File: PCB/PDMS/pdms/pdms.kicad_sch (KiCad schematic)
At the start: 46 parts, among them IC19 STM32L496ZGT6, IC20 AT25SF128A-SHB-T, J1 DBG, J2 12V_CONN, Y1 48Mhz, Y2 32KHz

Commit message: Mostly assigned footprints
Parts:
- removed J2: 12V_CONN, symbol Connector:Conn_01x01_Male

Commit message: Crucial fully assigned schematics
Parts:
- JP1: footprint (none) -> Jumper:SolderJumper-3_P1.3mm_Open_Pad1.0x1.5mm

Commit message: Added connector and more
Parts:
- added J2: 6473427-1, 64734271, symbol pdms_additional:6473427-1
- C41, C42, C43, C44, C45, C46, C47, C48, C49, C50, C51, C52, C53: footprint Capacitor_SMD:C_0402_1005Metric_Pad0.74x0.62mm_HandSolder -> Resistor_SMD:R_0402_1005Metric
- L1: footprint (none) -> Inductor_SMD:L_0402_1005Metric
- R108, R109, R55, R66: footprint Resistor_SMD:R_0402_1005Metric_Pad0.72x0.64mm_HandSolder -> Resistor_SMD:R_0402_1005Metric
- R54: footprint (none) -> Resistor_SMD:R_0805_2012Metric

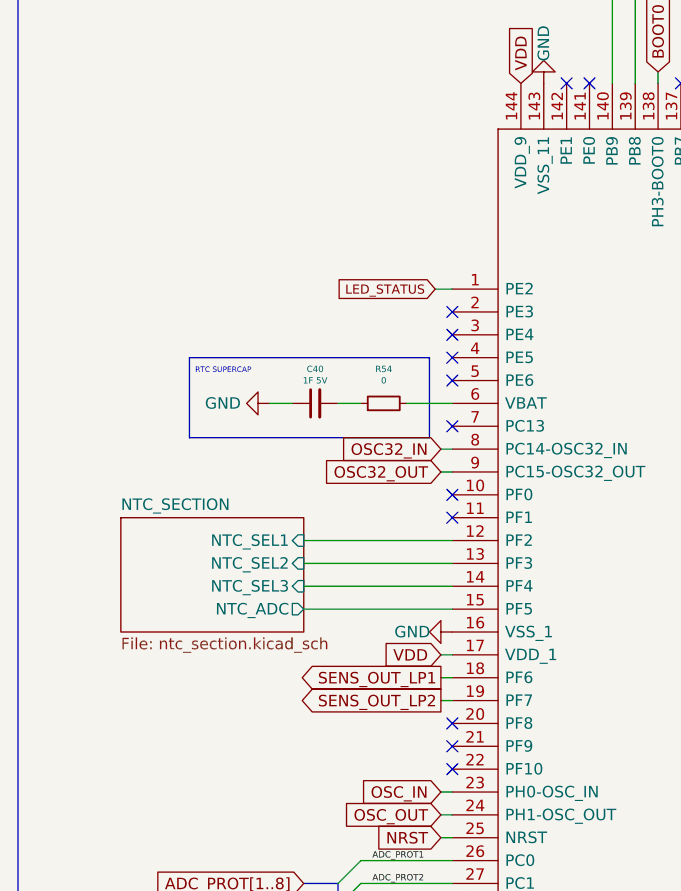
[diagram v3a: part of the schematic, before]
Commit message: Added voltage mux section & layouting high side - hp
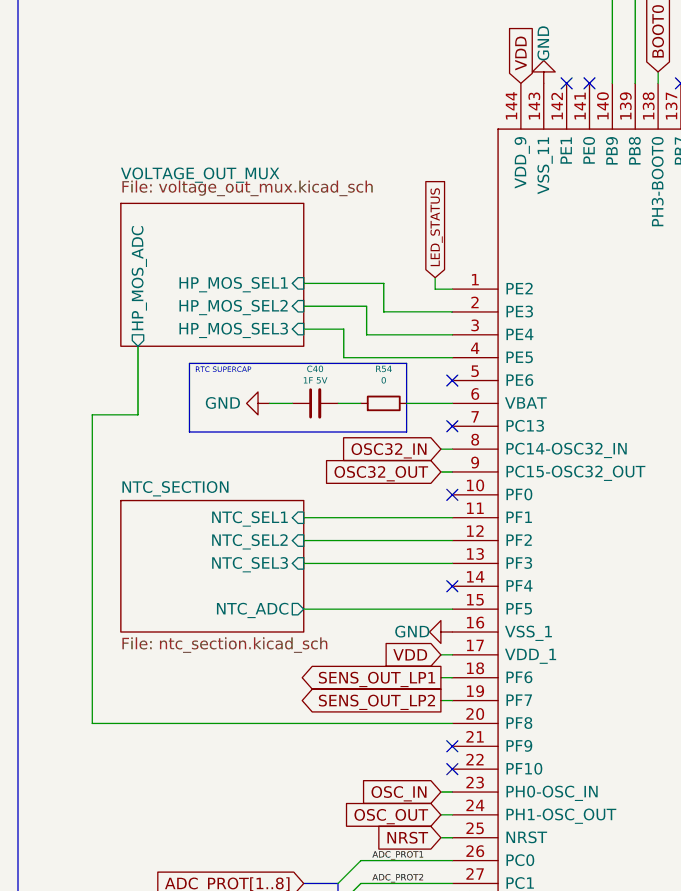
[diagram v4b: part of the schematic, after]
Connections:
- net NTC_SECTION/NTC_SEL1: now also IC19.11 (PF1); no longer IC19.12 (PF2)
- net NTC_SECTION/NTC_SEL2: now also IC19.12 (PF2); no longer IC19.13 (PF3)
- net NTC_SECTION/NTC_SEL3: now also IC19.13 (PF3); no longer IC19.14 (PF4)
- net VOLTAGE_OUT_MUX/HP_MOS_SEL1: now reaches IC19.2 (PE3)
- net VOLTAGE_OUT_MUX/HP_MOS_ADC: now reaches IC19.20 (PF8)
- net VOLTAGE_OUT_MUX/HP_MOS_SEL2: now reaches IC19.3 (PE4)
- net VOLTAGE_OUT_MUX/HP_MOS_SEL3: now reaches IC19.4 (PE5)
- no-connect marks 34 -> 30
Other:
- added sheet VOLTAGE_OUT_MUX (voltage_out_mux.kicad_sch)

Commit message: Medium power stage layout
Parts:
- J2: footprint 64734271 -> (none)
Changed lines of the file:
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@@
   (paper "A3")
   (bus_alias "QUADSPI" (members "CLK" "NCS" "BK1_IO0" "BK1_IO1" "BK1_IO2" "BK1_IO3"))
-  (bus_alias "SPI2" (members "SCK" "MISO" "MOSI"))
-  (bus_alias "SPI1" (members "SCK" "MOSI" "MISO"))
   (bus_alias "SPI3" (members "SCK" "MOSI" "MISO"))
+  (bus_alias "SPI1" (members "SCK" "MOSI" "MISO"))
+  (bus_alias "SPI2" (members "SCK" "MISO" "MOSI"))
   (junction (at 262.89 106.68) (diameter 0) (color 0 0 0 0)
   )
@@
     (property "Reference" "J2" (id 0) (at 368.3 158.75 0))
     (property "Value" "6473427-1" (id 1) (at 368.3 161.29 0))
-    (property "Footprint" "64734271" (id 2) (at 377.19 164.465 0)
+    (property "Footprint" "" (id 2) (at 377.19 164.465 0)
       (effects (font (size 1.27 1.27)) (justify left) hide)
     )
@@
     )
     (path "/1bbf27ea-c2a2-447a-8999-6ade1a66fd07/382312d4-d5fa-4b39-ace5-70b089c5702e/3370c7ea-69b3-4a24-9f00-dcee23cfca4d"
-      (reference "C14") (unit 1) (value "10nF") (footprint "Capacitor_SMD:C_0805_2012Metric")
+      (reference "C14") (unit 1) (value "10nF") (footprint "Capacitor_SMD:C_0603_1608Metric")
     )
     (path "/1bbf27ea-c2a2-447a-8999-6ade1a66fd07/382312d4-d5fa-4b39-ace5-70b089c5702e/ea05a7b0-a751-41e9-9025-7282beaf4e1d"
-      (reference "C15") (unit 1) (value "10nF") (footprint "Capacitor_SMD:C_0805_2012Metric")
+      (reference "C15") (unit 1) (value "10nF") (footprint "Capacitor_SMD:C_0603_1608Metric")
     )
     (path "/1bbf27ea-c2a2-447a-8999-6ade1a66fd07/382312d4-d5fa-4b39-ace5-70b089c5702e/1d67a290-67f8-4c45-a531-ecadc3675a3a"
-      (reference "C16") (unit 1) (value "10nF") (footprint "Capacitor_SMD:C_0805_2012Metric")
+      (reference "C16") (unit 1) (value "10nF") (footprint "Capacitor_SMD:C_0603_1608Metric")
     )
     (path "/1bbf27ea-c2a2-447a-8999-6ade1a66fd07/382312d4-d5fa-4b39-ace5-70b089c5702e/5bf50f4d-56e9-48bb-98a7-9ba919c6cef3"
-      (reference "C17") (unit 1) (value "10nF") (footprint "Capacitor_SMD:C_0805_2012Metric")
+      (reference "C17") (unit 1) (value "10nF") (footprint "Capacitor_SMD:C_0603_1608Metric")
     )
     (path "/1bbf27ea-c2a2-447a-8999-6ade1a66fd07/382312d4-d5fa-4b39-ace5-70b089c5702e/a56d669c-c591-4097-b59f-91a85033a48d"
@@
     )
     (path "/1bbf27ea-c2a2-447a-8999-6ade1a66fd07/3f236385-25de-4e3f-a771-f7ba7d7dd03b/3370c7ea-69b3-4a24-9f00-dcee23cfca4d"
-      (reference "C70") (unit 1) (value "10nF") (footprint "Capacitor_SMD:C_0805_2012Metric")
+      (reference "C70") (unit 1) (value "10nF") (footprint "Capacitor_SMD:C_0603_1608Metric")
     )
     (path "/1bbf27ea-c2a2-447a-8999-6ade1a66fd07/3f236385-25de-4e3f-a771-f7ba7d7dd03b/ea05a7b0-a751-41e9-9025-7282beaf4e1d"
-      (reference "C71") (unit 1) (value "10nF") (footprint "Capacitor_SMD:C_0805_2012Metric")
+      (reference "C71") (unit 1) (value "10nF") (footprint "Capacitor_SMD:C_0603_1608Metric")
     )
     (path "/1bbf27ea-c2a2-447a-8999-6ade1a66fd07/3f236385-25de-4e3f-a771-f7ba7d7dd03b/1d67a290-67f8-4c45-a531-ecadc3675a3a"
-      (reference "C72") (unit 1) (value "10nF") (footprint "Capacitor_SMD:C_0805_2012Metric")
+      (reference "C72") (unit 1) (value "10nF") (footprint "Capacitor_SMD:C_0603_1608Metric")
     )
     (path "/1bbf27ea-c2a2-447a-8999-6ade1a66fd07/3f236385-25de-4e3f-a771-f7ba7d7dd03b/5bf50f4d-56e9-48bb-98a7-9ba919c6cef3"
-      (reference "C73") (unit 1) (value "10nF") (footprint "Capacitor_SMD:C_0805_2012Metric")
+      (reference "C73") (unit 1) (value "10nF") (footprint "Capacitor_SMD:C_0603_1608Metric")
     )
     (path "/f973e110-c9eb-4494-a7eb-37628bac99f8/808924b7-27d2-4209-a500-7d9830d3c986"
@@
     )
     (path "/3e968dc6-4b4f-40cc-bb81-01963d659485"
-      (reference "J2") (unit 1) (value "6473427-1") (footprint "64734271")
+      (reference "J2") (unit 1) (value "6473427-1") (footprint "")
     )
     (path "/2ac18ad3-7152-47d9-8b69-5b63b2971d75"

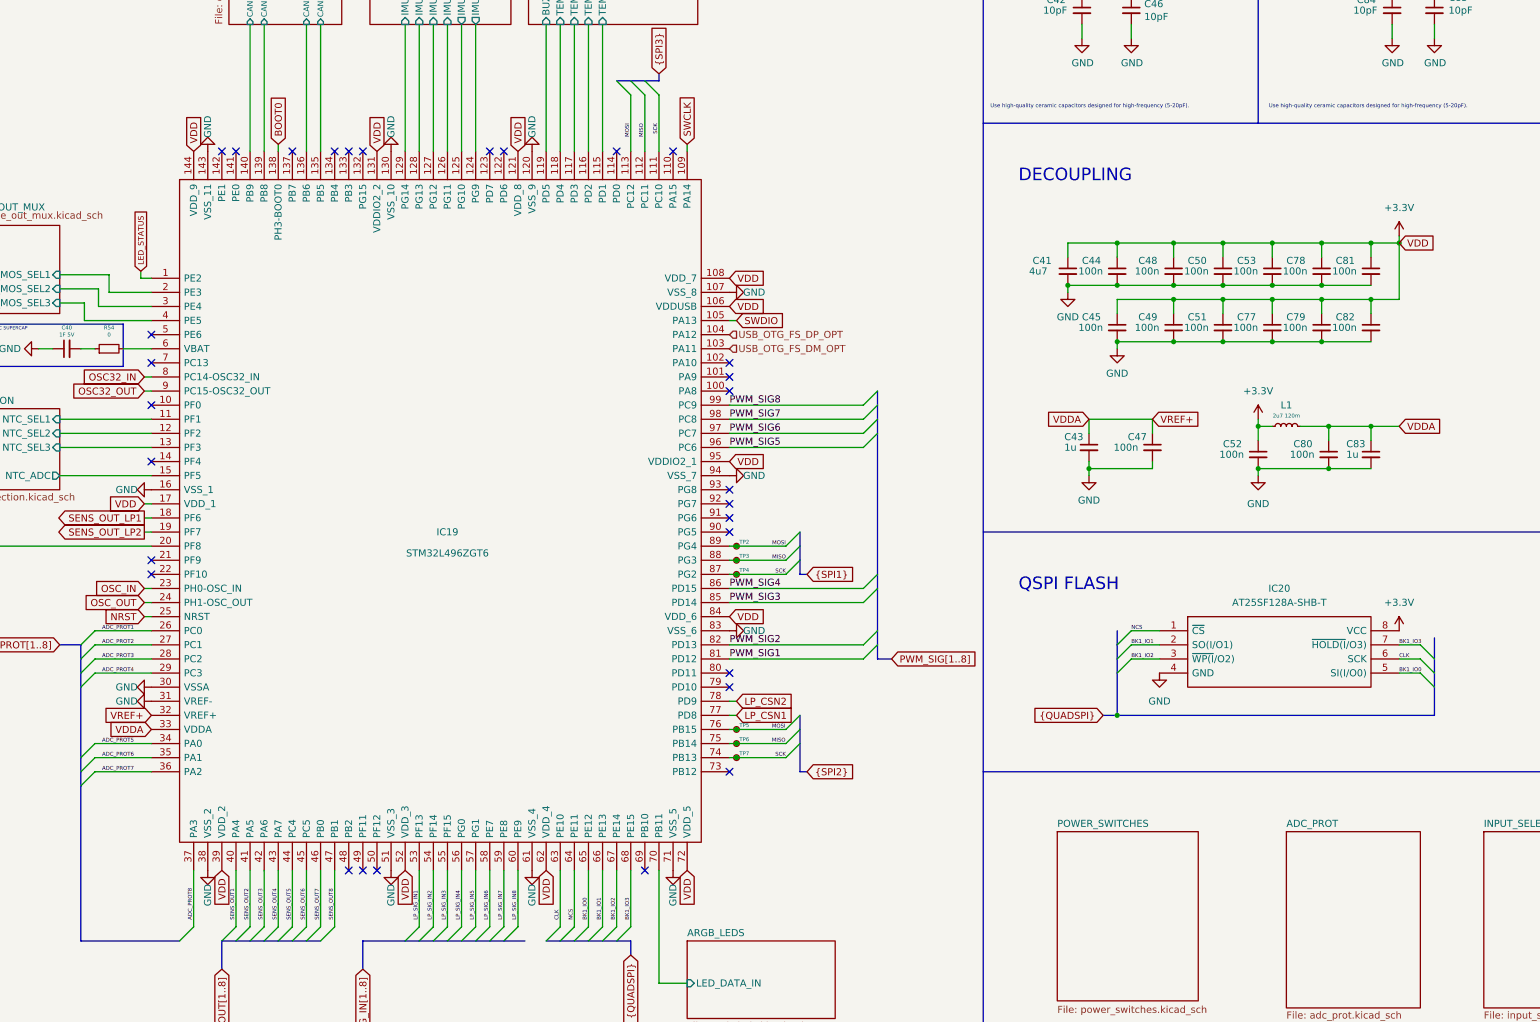
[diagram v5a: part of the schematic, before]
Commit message: Imported 3.3V section with problematic shitty plugin
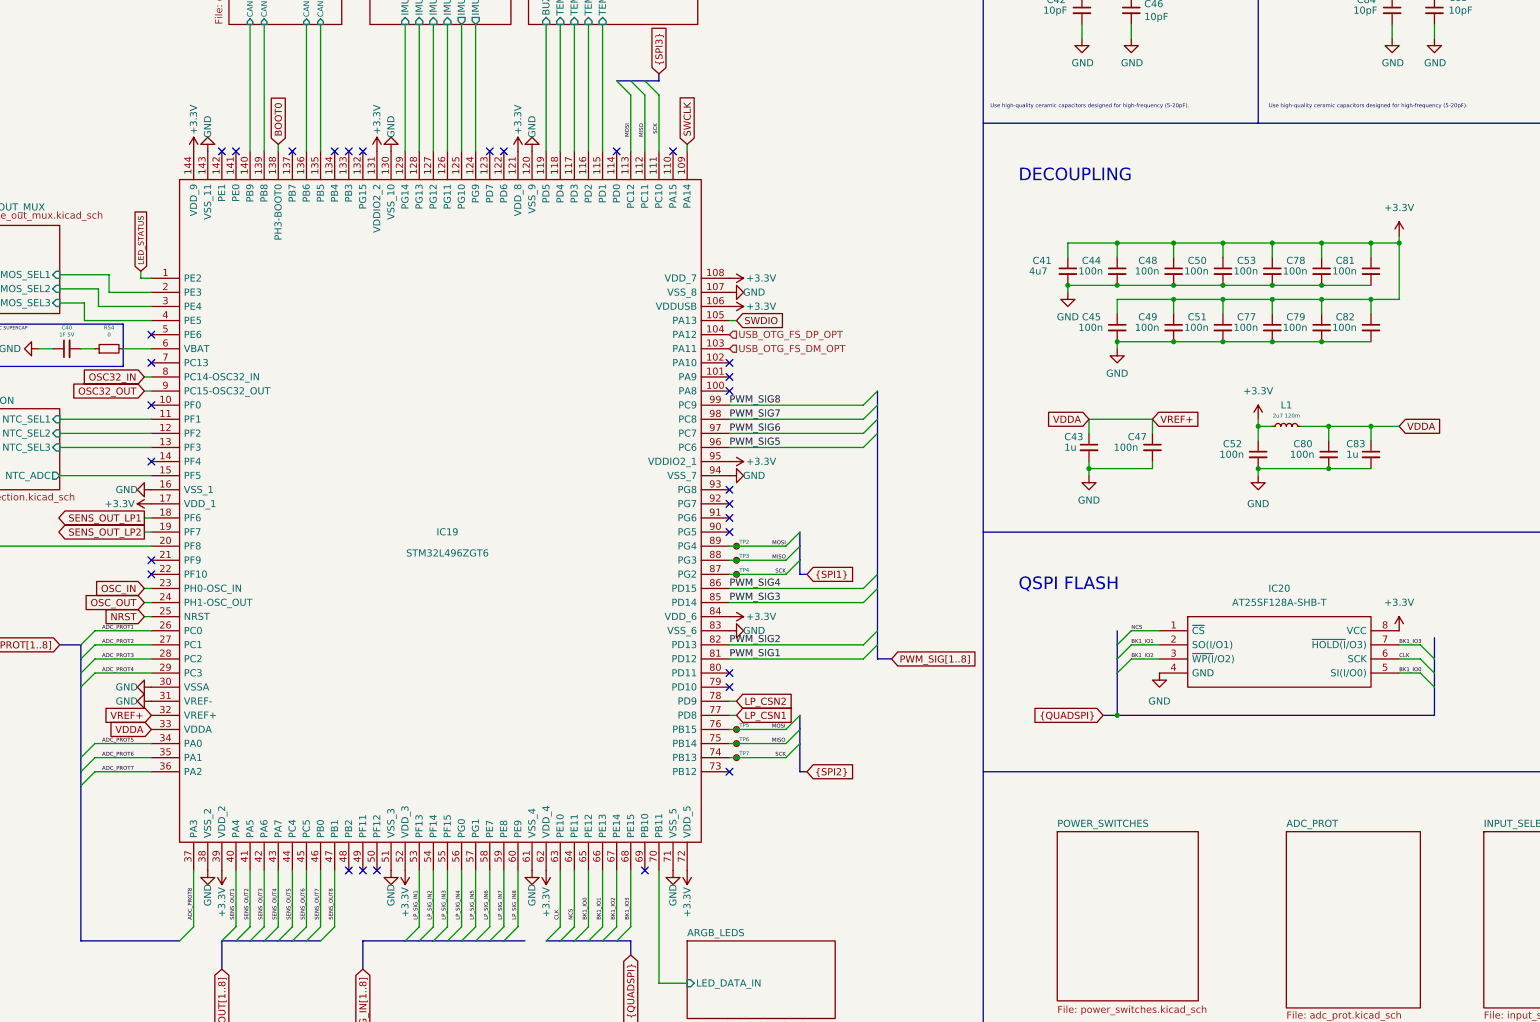
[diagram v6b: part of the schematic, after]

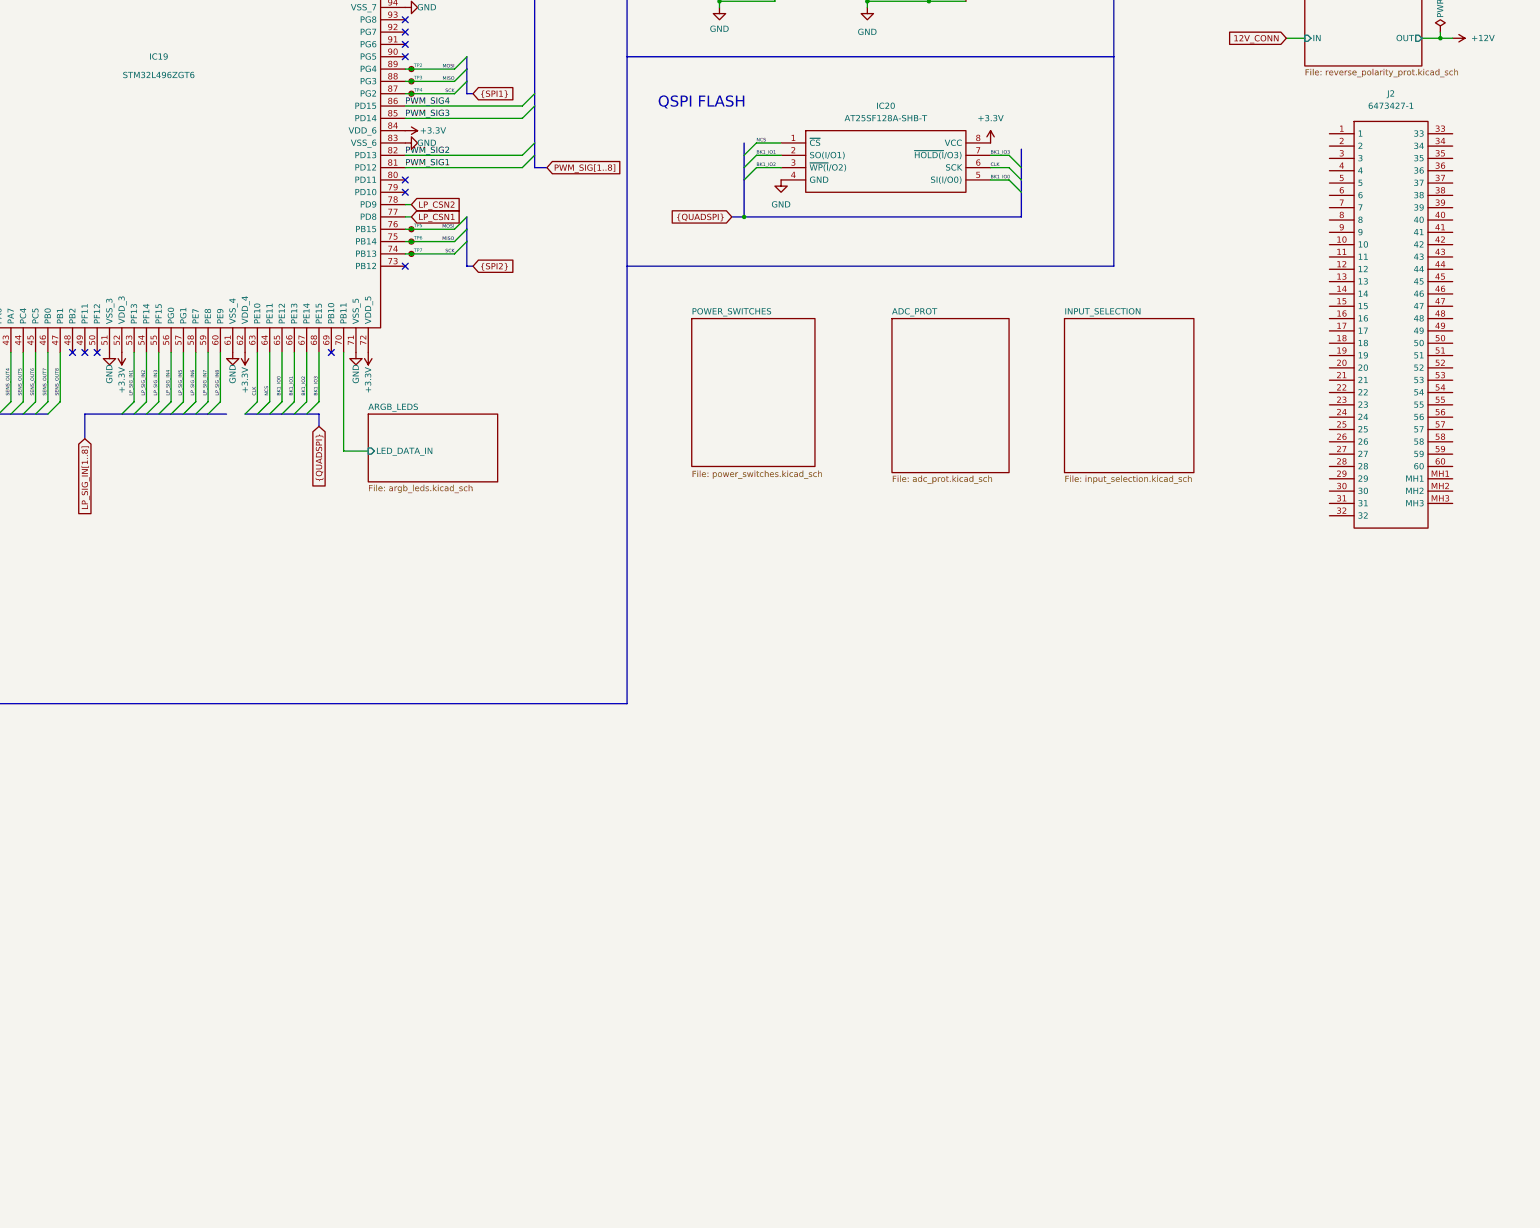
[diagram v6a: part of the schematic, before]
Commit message: Layout of high current traces to connector changed
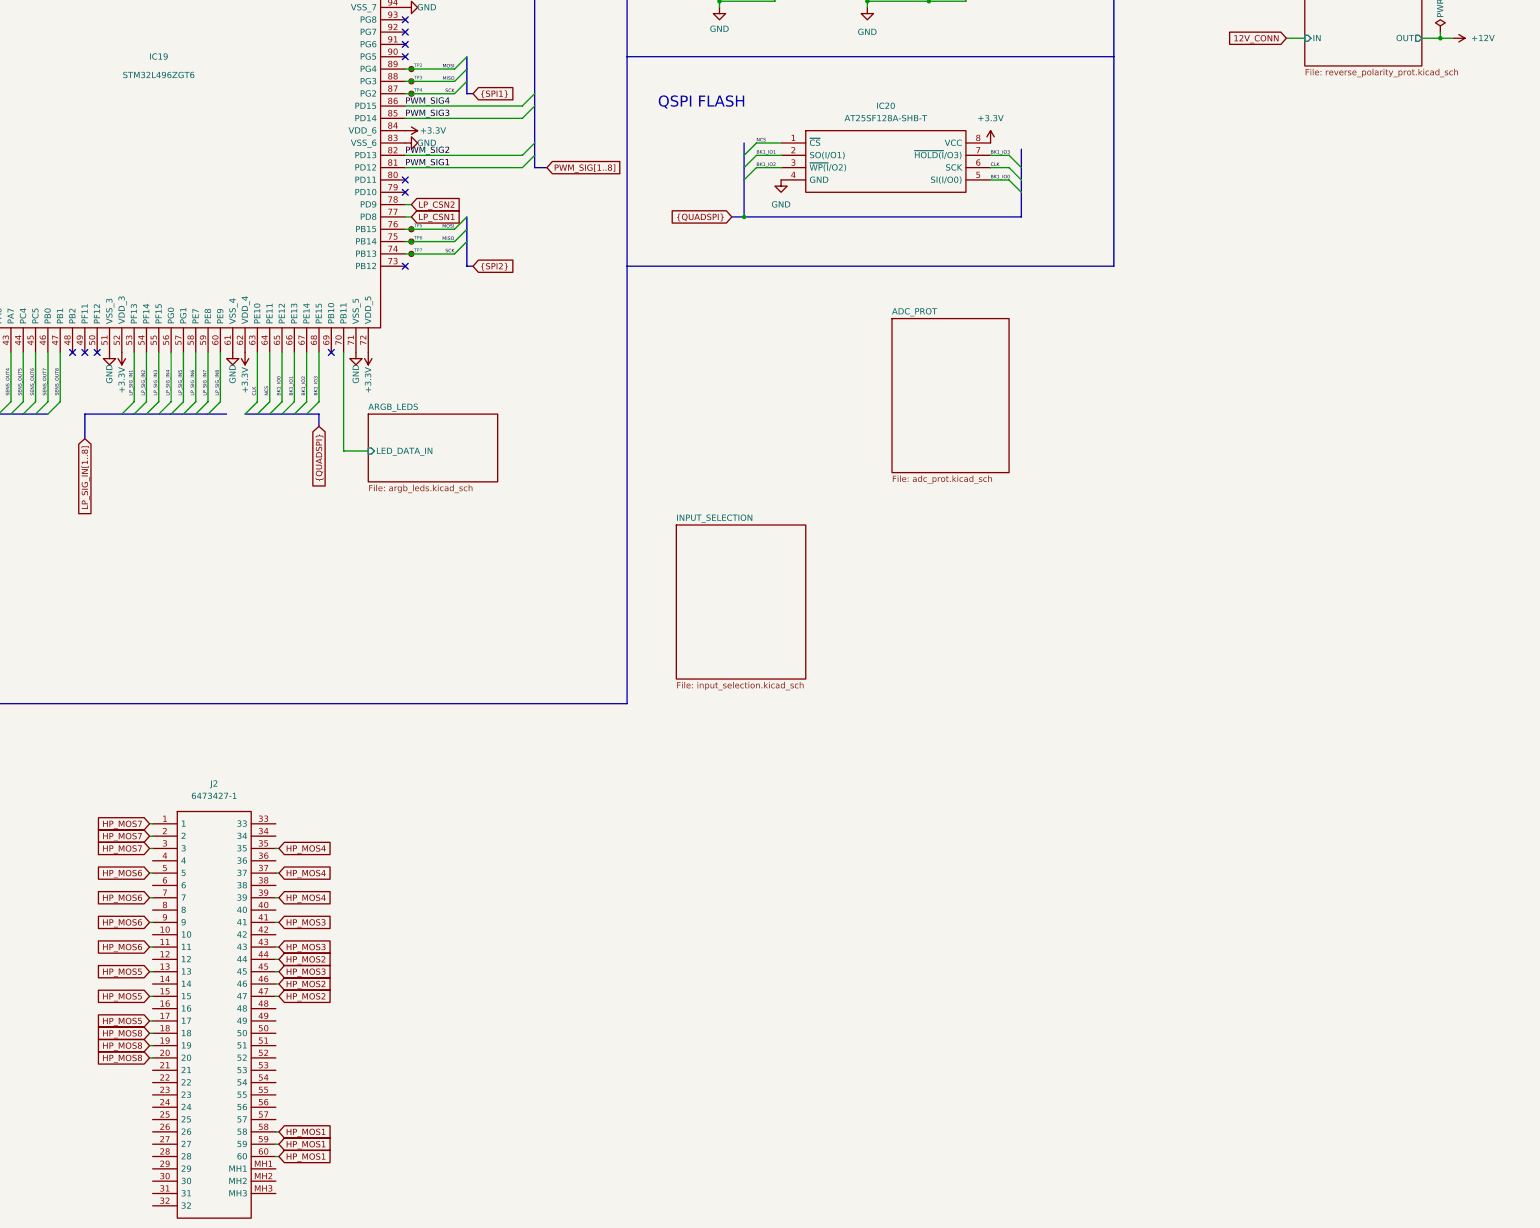
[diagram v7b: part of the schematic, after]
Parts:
- J2: footprint (none) -> PDMS_Additional:64734271
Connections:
- net HP_MOS7: now reaches J2.1
- net HP_MOS7: now also J2.2, J2.3
- net HP_MOS6: now reaches J2.11
- net HP_MOS6: now also J2.5, J2.7, J2.9
- net HP_MOS5: now reaches J2.13
- net HP_MOS5: now also J2.15, J2.17
- net HP_MOS8: now reaches J2.18
- net HP_MOS8: now also J2.19, J2.20
- net HP_MOS4: now reaches J2.35
- net HP_MOS4: now also J2.37, J2.39
- net HP_MOS3: now reaches J2.41
- net HP_MOS3: now also J2.43, J2.45
- net HP_MOS2: now reaches J2.44
- net HP_MOS2: now also J2.46, J2.47
- net HP_MOS1: now reaches J2.58
- net HP_MOS1: now also J2.59, J2.60
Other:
- removed sheet POWER_SWITCHES
- moved on the sheet: J2
